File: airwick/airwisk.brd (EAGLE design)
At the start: 45 x 22 mm, 14 parts, among them IC1 LF33CDt, K1 G5V-2, T1 2N2222A

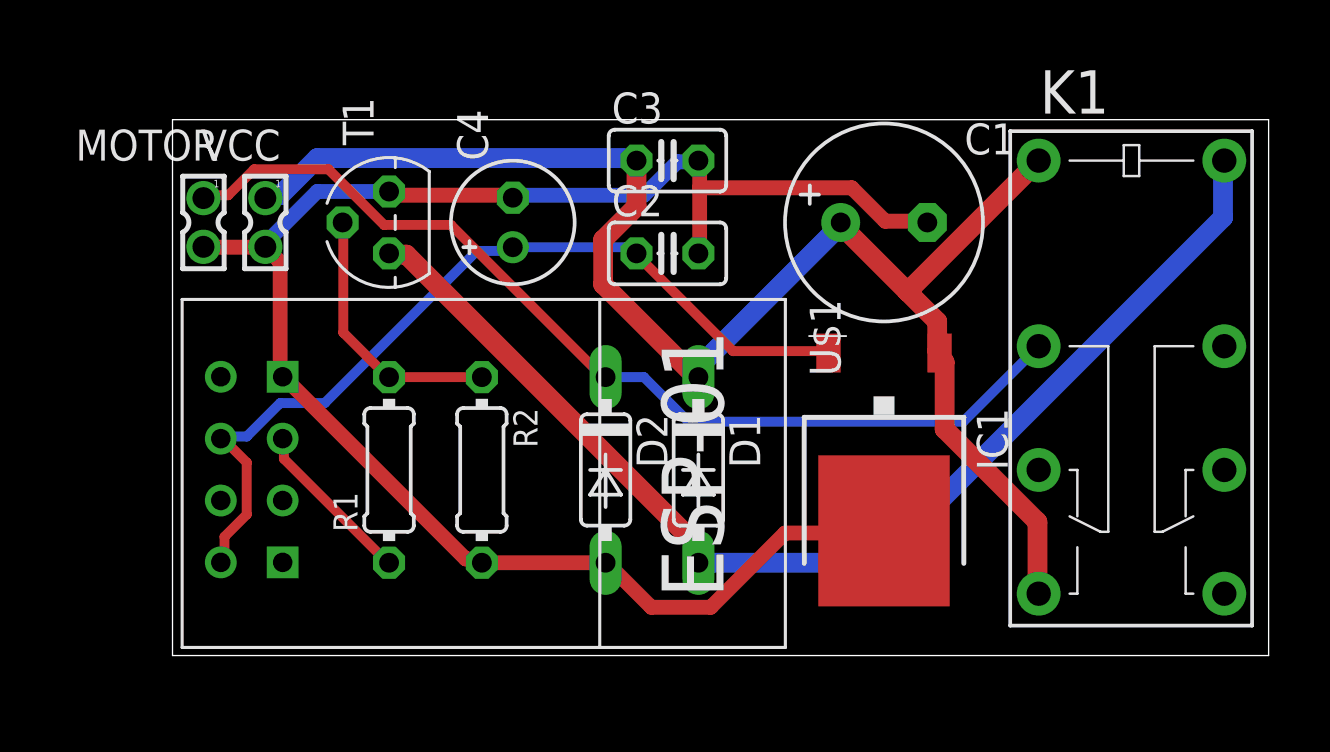
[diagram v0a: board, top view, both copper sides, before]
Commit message: update R1  to 47k and delete R2 => for GPO02 to low
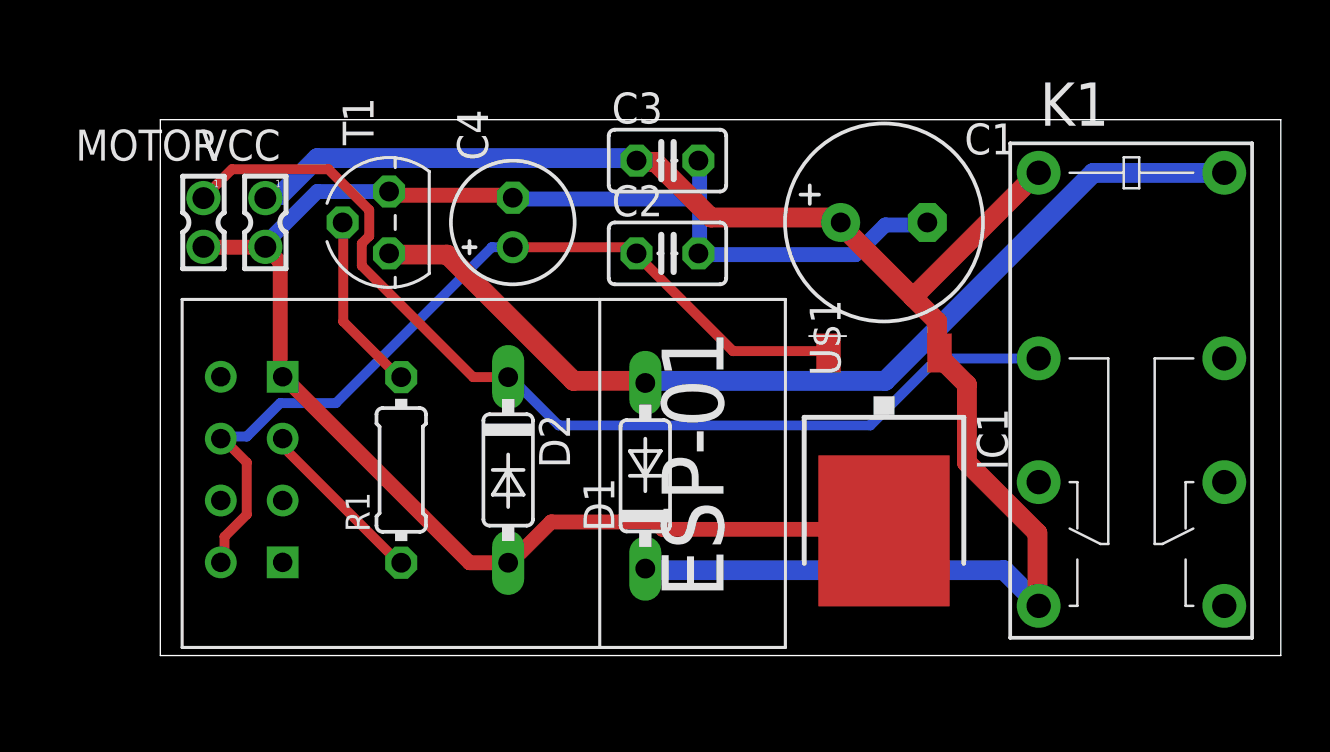
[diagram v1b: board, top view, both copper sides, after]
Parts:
- removed R2: 220Ω, resistor:0204/7
- R1: value 220Ω -> 47K
- moved D2 4.00 mm to (13.8, 7.62)
- moved D1 2.19 mm to (19.4, 7.38), turned to 90 degrees
- moved K1 0.50 mm to (39.4, 10.9)
- moved R1 0.50 mm to (9.39, 7.62)
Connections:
- net GND: no longer R2.2
- net N$3: no longer R2.1
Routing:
- net N$4: track 48.2 -> 40.1 mm
- net N$1: track 62.2 -> 68.7 mm
- net N$3: track 11.0 -> 7.39 mm
- net GND: track 71.4 -> 69.6 mm
- net N$2: track 40.4 -> 42.0 mm
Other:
- board size 45 x 22 mm -> 46 x 22 mm
